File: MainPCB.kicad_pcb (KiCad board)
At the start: 4 copper layers, 128 x 89.5 mm, 105 parts, among them IC1 VNH7070ASTR, IC2 VNH7070ASTR, IC3 VNH7070ASTR, IC4 VNH7070ASTR, IC5 VNH7070ASTR, J1 Conn_01x06, J10 Conn_01x02, J101 TYPEC-305-ACP16H458, J11 Conn_01x03, J2 Conn_01x05_Pin, J20 Conn_01x02_Pin, J3 Conn_01x12, J4 Conn_01x02, J5 Screw_Terminal_01x02, J501 GT-HD001B-CNNG1, J8 Conn_01x02, J802 Conn_01x22_Female, J9 Conn_01x02, M1 Motor_DC, M2 Motor_DC, M3 Motor_DC, M4 Motor_DC, M5 Motor_DC, SW1 SW_DPST_x2, SW6 SW_DPST_x2, T401 7498111120AR, U10 N channel, U12 Teensy4.1, U3 BoostConverter, U4 BNO055, U401 TPD4EUSB30, U402 TPD4EUSB30, U405 STMPS2151STR, U6 N channel, U602 SN74LVC1G14DBVR, U701 AP22653W6

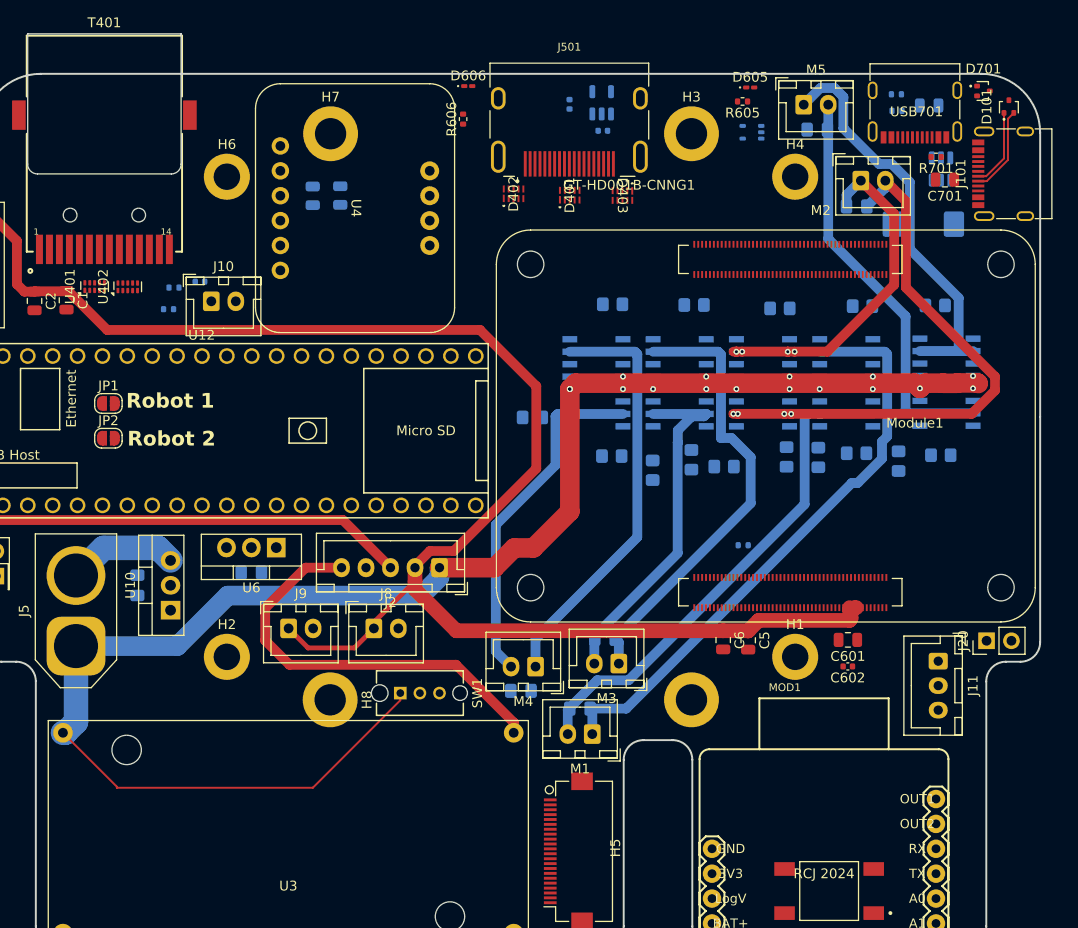
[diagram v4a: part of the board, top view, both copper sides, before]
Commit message: Finished Routing Diff Pairs
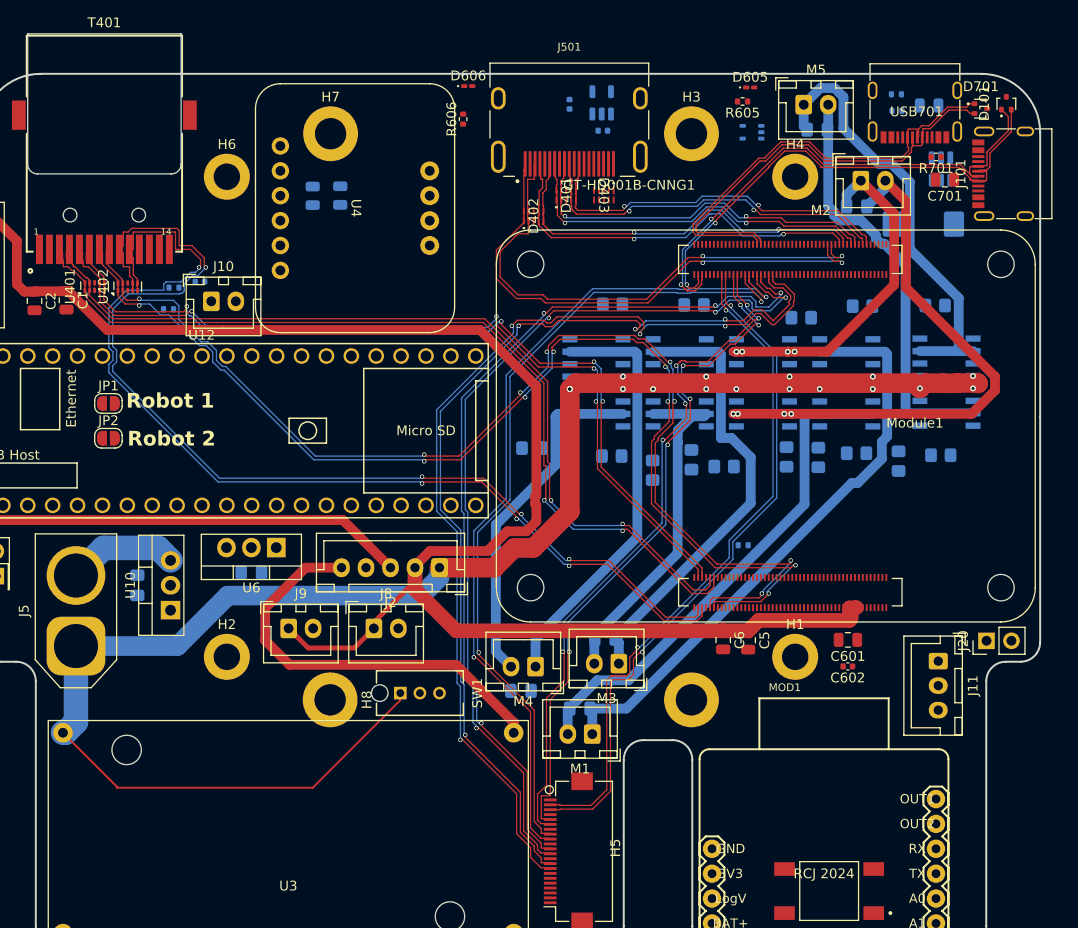
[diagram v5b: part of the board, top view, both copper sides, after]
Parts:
- moved R17 3.13 mm to (102.1, 103.2)
- moved D402 3.05 mm to (102.3, 79.5)
- moved R9 2.38 mm to (129.6, 89.9)
- moved D403 1.90 mm to (109.5, 77.4)
- moved D701 1.82 mm to (147.9, 68.5)
- moved D101 0.43 mm to (150.6, 68.0)
- moved D401 0.36 mm to (105.6, 77.4)
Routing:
- net /CM5/ETH_PI.TRD2_N: track 0.00 -> 120.8 mm, vias 0 -> 8
- net /CM5/ETH_PI.TRD2_P: track 0.00 -> 120.7 mm, vias 0 -> 8
- net /CM5/ETH_PI.TRD3_P: track 0.00 -> 108.5 mm, vias 0 -> 4
- net /CM5/ETH_PI.TRD3_N: track 0.00 -> 107.5 mm, vias 0 -> 4
- net /CM5/DPHY0_P.D3_P: track 0.00 -> 102.5 mm, vias 0 -> 4
- net /CM5/DPHY0_P.D3_N: track 0.00 -> 99.8 mm, vias 0 -> 4
- net /CM5/DPHY0_P.D2_N: track 0.00 -> 93.1 mm, vias 0 -> 4
- net /CM5/DPHY0_P.D2_P: track 0.00 -> 93.0 mm, vias 0 -> 4
- net /CM5/ETH_PI.TRD0_P: track 0.00 -> 91.8 mm, vias 0 -> 2
- net /CM5/ETH_PI.TRD0_N: track 0.00 -> 90.0 mm, vias 0 -> 2
- net /CM5/ETH_PI.TRD1_N: track 0.00 -> 87.7 mm, vias 0 -> 4
- net /CM5/ETH_PI.TRD1_P: track 0.00 -> 87.7 mm, vias 0 -> 4
- net /CM5/DPHY0_P.C_P: track 0.00 -> 86.3 mm, vias 0 -> 2
- net /CM5/DPHY0_P.C_N: track 0.00 -> 84.9 mm, vias 0 -> 2
- net /CM5/DPHY0_P.D1_P: track 0.00 -> 71.0 mm, vias 0 -> 6
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
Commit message: Fixed some errors
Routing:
- net Net-(U3-In-): track 0.00 -> 55.6 mm, vias 0 -> 6
- net /USB_C.D_N: track 52.5 -> 53.5 mm

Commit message: Did a bunch of routing, freerouting is broken, and im lowk tired
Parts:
- moved R12 6.33 mm to (113.9, 84.4)
- moved R14 5.66 mm to (119.0, 108.9)
- moved R15 3.61 mm to (109.2, 85.1)
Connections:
- R3 pad 1: DIR4A -> DIR5A
- R4 pad 1: DIR4B -> DIR5B
- R5 pad 2: PWM4 -> PWM5
- U12 pad 2: LEDPulse -> unconnected-(U12-0_RX1_CRX2_CS1-Pad2)
- U12 pad 3: ESC_PWM -> unconnected-(U12-1_TX1_CTX2_MISO1-Pad3)
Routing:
- net 3.3V: track 66.1 -> 203.0 mm, vias 0 -> 2
- net SCL2: track 0.00 -> 129.1 mm
- net PWM5: track 0.00 -> 122.4 mm, vias 0 -> 1
- net SDA2: track 0.00 -> 120.8 mm
- net UART3_CTS -> RTS: track 0.00 -> 110.3 mm, vias 0 -> 1
- net PWM1: track 0.00 -> 109.4 mm, vias 0 -> 3
- net RX3->TX: track 0.00 -> 109.0 mm, vias 0 -> 1
- net TX7 -> RX: track 0.00 -> 101.6 mm
- net DIR1A: track 0.00 -> 99.7 mm, vias 0 -> 1
- net RX7 -> TX: track 0.00 -> 98.8 mm
- net DIR2B: track 0.00 -> 97.5 mm, vias 0 -> 1
- net DIR1B: track 0.00 -> 92.8 mm, vias 0 -> 1
- net DIR2A: track 0.00 -> 86.5 mm, vias 0 -> 1
- net Net-(SW6A-B): track 0.00 -> 86.1 mm, vias 0 -> 1
- net CS6: track 0.00 -> 85.4 mm
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- added copper zone on B.Cu, net GND
- added copper zone on F.Cu, net GND
- added copper zone on In1.Cu, net GND
- added copper zone on In2.Cu, net GND
- added copper zone on In3.Cu, net GND
- added copper zone on In4.Cu, net GND
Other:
- outline, holes or cut-outs redrawn
- copper layers 4 -> 6
